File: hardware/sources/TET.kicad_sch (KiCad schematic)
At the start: 68 parts, among them J1 SWT, M1 MountingHole, M2 MountingHole, M3 MountingHole, M4 MountingHole, U1 E80-900M2213S_C42464134, U10 STM32L431RBT6TR, U12 TCAN330GDCNR, U13 SMA_1, U14 SMA_2, U15 8 MHz, U16 5015, U17 5015, U18 5015, U2 STM32L431CBT6, U3 W25Q128JVSIQTR, U4 W25Q128JVSIQTR, U5 W25Q128JVSIQTR, U6 TMP112AIDRLR, U7 TMP112AIDRLR, U8 TMP112AIDRLR, U9 TMP112AIDRLR

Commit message: hardware(schematics): upload pre-review schematic
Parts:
- removed C1, C14, C15, C16, C17, C18, C19: 100nF, Capacitor_SMD:C_0603_1608Metric, symbol Device:C_Small
- removed C20: 10uF, Capacitor_SMD:C_0603_1608Metric, symbol Device:C_Small
- removed C21: 10nF, Capacitor_SMD:C_0603_1608Metric, symbol Device:C_Small
- removed C22, C23: 1uF, Capacitor_SMD:C_0603_1608Metric, symbol Device:C_Small
- removed C8: 0.1uF, Capacitor_SMD:C_0603_1608Metric, symbol Device:C_Small
- removed D4: ON_LED, LED_SMD:LED_0805_2012Metric, symbol Device:LED
- removed D5: TX_LED, LED_SMD:LED_0805_2012Metric, symbol Device:LED
- removed D6: RX_LED, LED_SMD:LED_0805_2012Metric, symbol Device:LED
- removed J1: SWT, Connector_PinHeader_2.54mm:PinHeader_1x04_P2.54mm_Vertical, symbol Connector_Generic:Conn_01x04
- removed R3, R4: 10k, symbol Device:R_Small
- removed R6: 5k, Resistor_SMD:R_0603_1608Metric, symbol Device:R_Small
- removed U1: E80-900M2213S_C42464134, TET-Footprints:WIFIM-SMD_22P-L26.0-W16.0-P1.27-TL, symbol TET-Symbols:E80-900M2213S_C42464134
- removed U13: SMA_1, TET-Footprints:SMA-TH_SMA-KWE_C7498154, symbol TET-Symbols:SMA-KWE_C7498154
- removed U14: SMA_2, TET-Footprints:SMA-TH_SMA-KWE_C7498154, symbol TET-Symbols:SMA-KWE_C7498154
- removed U15: 8 MHz, TET-Footprints:CRYSTAL-SMD_L5.0-W3.2, symbol TET-Symbols:X50328MSB2GI
- removed U16, U17, U18: 5015, TET-Footprints:TEST-SMD_L2.7-W1.0, symbol TET-Symbols:5015
- removed U2: STM32L431CBT6, TET-Footprints:LQFP-48_L7.0-W7.0-P0.50-LS9.0-BL, symbol TET-Symbols:STM32L431CBT6
- removed U3, U4, U5: W25Q128JVSIQTR, TET-Footprints:SOIC-8_L5.3-W5.3-P1.27-LS8.0-BL, symbol TET-Symbols:W25Q128JVSIQTR
- removed U6, U8, U9: TMP112AIDRLR, TET-Footprints:SOT-563_L1.6-W1.2-P0.50-LS1.6-BR, symbol TET-Symbols:TMP112AIDRLR
- added C11: 10nF, Capacitor_SMD:C_0603_1608Metric, symbol Device:C_Small
- added C12: 1uF, Capacitor_SMD:C_0603_1608Metric, symbol Device:C_Small
- added C5: 100nF, Capacitor_SMD:C_0603_1608Metric, symbol Device:C_Small
- added J1: SWD, Connector_PinHeader_2.54mm:PinHeader_1x06_P2.54mm_Vertical, symbol Connector_Generic:Conn_01x06
- added R16: 10k, Resistor_SMD:R_0603_1608Metric, symbol Device:R_Small
- added R17, R7: 4.7k, Resistor_SMD:R_0603_1608Metric, symbol Device:R_Small
- added U2: 8 MHz, TET-Footprints:CRYSTAL-SMD_L5.0-W3.2, symbol TET-Symbols:X50328MSB2GI
- C10, C6, C7, C9: value 0.1uF -> 100nF
- C13: value 22uF -> 1uF
- C3: value 20pF -> 100nF
- C4: value 0.1uF -> 20pF
- FB1: LCSC C14709 -> (none)
- R1, R2, R5: footprint (none) -> Resistor_SMD:R_0603_1608Metric
- R10: value 200 -> 33
- R11: value 82 -> 33
- R12, R13: value 10k -> 33
- R14: value 10k -> 4.7k
- R15: value 5k -> 10k
- R3: renamed from R16; footprint Resistor_SMD:R_0805_2012Metric_Pad1.20x1.40mm_HandSolder -> Resistor_SMD:R_0603_1608Metric
- R4: renamed from R17; footprint Resistor_SMD:R_0805_2012Metric_Pad1.20x1.40mm_HandSolder -> Resistor_SMD:R_0603_1608Metric
- R6: renamed from R7; value 5k -> 4.7k
- R8: value 5k -> 4.7k
- R9: value 270 -> 33
- renumbered C11 to C1, C5 to C14, C12 to C8, U12 to U1, U10 to U3, U7 to U4
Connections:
- net BOOT0 is gone; now on net LR_NSS: R1.2
- net OSC_IN is gone; now on an unnamed net: C2.1
- net OSC_OUT is gone; now on net +3.3V: C3.1
- net TMP112_A_ALERT is gone; now on net I2C2_SCL: R8.2
- net +3.3V: now also R1.1, U3.1 (VBAT), U3.19 (VDD), U3.32 (VDD), U3.48 (VDD), U3.64 (VDD), C5.1, J1.1 (Pin_1), R16.1, R17.1, R7.1; no longer C4.1, C6.1, R12.1, R13.1, R5.1
- net +3.3VA: now also U3.13 (VDDA/VREF+), C11.1, C12.1
- net CAN1_RX: now also U3.44 (PA11)
- net CAN1_STB: now also U3.28 (PB2)
- net CAN1_TX: now also U3.45 (PA12)
- net FLASH1_CS: now also R15.2, U3.33 (PB12); no longer R12.2
- net FLASH2_CS: now also U3.34 (PB13), R16.2; no longer R13.2
- net FLASH3_CS: now also R18.2, U3.36 (PB15); no longer R14.2
- net GND: now also R5.1, U3.12 (VSSA/VREF-), U3.18 (VSS), U3.31 (VSS), U3.47 (VSS), U3.63 (VSS), C11.2, C12.2, C5.2, J1.6 (Pin_6); no longer R1.1, R10.1, R11.1, R9.1
- net I2C1_SCL: now also U3.58 (PB6), R7.2
- net I2C1_SDA: now also R14.2, U3.59 (PB7)
- net LR_BUSY: now also U3.40 (PC9)
- net LR_IO7: now also U3.52 (PC11)
- net LR_IO8: now also U3.53 (PC12)
- net LR_IO9: now also U3.2 (PC13)
- net LR_NSS: now also U3.51 (PC10)
- net LR_RST: now also R2.2, U3.39 (PC8); no longer R18.2
- net NRST: now also C6.1, U3.7 (NRST), J1.4 (Pin_4)
- net QSPI_CLK: now also R9.2
- net QSPI_IO0: now also R13.2
- net QSPI_IO1: now also R12.2
- net QSPI_IO2: now also R11.2
- net QSPI_IO3: now also R10.2
- net RX_LED: now also U3.9 (PC1)
- net SPI1_MISO: now also U3.56 (PB4)
- net SPI1_MOSI: now also U3.57 (PB5)
- net SPI1_SCK: now also U3.15 (PA1)
- net SWCLK: now also U3.49 (PA14), J1.3 (Pin_3)
- net SWDIO: now also U3.46 (PA13), J1.2 (Pin_2)
- net TX_LED: now also U3.8 (PC0)
- net RF_INA_ALERT: now reaches U3.14 (PA0)
- net TMP_B_ALERT: now reaches U3.16 (PA2)
- net TMP_B_ALERT: now also R6.2, U4.3 (ALERT)
- net at U3.17 (PA3): now also R9.1
- net TMP_C_ALERT: now reaches U3.20 (PA4)
- net TMP_D_ALERT: now reaches U3.21 (PA5)
- net at U3.22 (PA6): now also R10.1
- net at U3.23 (PA7): now also R11.1
- net UART_B_TX: now reaches U3.24 (PC4)
- net UART_B_RX: now reaches U3.25 (PC5)
- net at U3.26 (PB0): now also R12.1
- net at U3.27 (PB1): now also R13.1
- net I2C2_SCL: now reaches U3.29 (PB10)
- net I2C2_SDA: now reaches U3.35 (PB14)
- net I2C2_SDA: now also R17.2
- net PWR_INA_ALERT: now reaches U3.37 (PC6)
- net TMP_A_ALERT: now reaches U3.38 (PC7)
- net UART_A_TX: now reaches U3.42 (PA9)
- net UART_A_RX: now reaches U3.43 (PA10)
- net at U3.5 (PH0/OSCIN): now also U2.2 (OSC2)
- net SWO: now reaches U3.55 (PB3)
- net SWO: now also J1.5 (Pin_5)
- net at U3.6 (PH1/OSCOUT): now also C4.1, U2.1 (OSC1)
- net at U3.60 (PH3/BOOT0): now also R5.2
- removed net TMP112_B_ALERT: R5.2, R6.2, U4.3 (ALERT)
- removed net TMP112_D_ALERT: R15.2, R2.2
- no-connect marks 6 -> 10
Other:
- added sheet RF_Transceiver (TET-RF-Transceiver.kicad_sch)
- sheet Power_Supply ports: added CAN_A_H, CAN_A_L, I2C1_SCL, I2C1_SDA, PWR_INA_ALERT, RX_LED, TMP_A_ALERT, TX_LED, UART_A_RX, UART_A_TX, UART_B_RX, UART_B_TX; removed none
- note added: "MCU"
- note added: "MECHANICAL HOLES"
- note added: "OPEN HARDWARE"
- note removed: "1x CAN BUS 1x UART 1x SPI 1x QUADSPI 1x I2C"
- note removed: "Adicionar resistores de terminação + pull up nas linhas QSPI"
- note removed: "CL = 2*(CL0-Cs) = 2*(20pF-10pF) = 20pF"
- note removed: "GREEN"
- note removed: "PULL UP 4.7K"
- note removed: "RED"
- note removed: "YELLOW"
- moved on the sheet: C1, C14, C8, M1, M2, M3, M4, R3, R4, R6, U1, U3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

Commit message: hardware(schematic): link datasheet to all main components #1
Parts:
- FB1: LCSC (none) -> C14709
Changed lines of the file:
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@@
 			)
 		)
-		(property "Datasheet" "https://atta.szlcsc.com/upload/public/pdf/source/20201224/C1509088_801C146548210414D75CA4C6AF5FD003.pdf"
+		(property "Datasheet" "https://www.ti.com/lit/gpn/TCAN330G"
 			(at 53.594 182.753 0)
 			(effects
@@
 			)
 		)
-		(property "Datasheet" "https://item.szlcsc.com/188416.html"
+		(property "Datasheet" "https://www.ti.com/lit/gpn/TMP112"
 			(at 185.674 143.383 0)
 			(effects
@@
 			)
 		)
-		(property "Datasheet" "~"
+		(property "Datasheet" "https://www.lcsc.com/datasheet/C14709.pdf"
 			(at 166.37 27.94 0)
 			(effects
@@
 			)
 		)
+		(property "LCSC" "C14709"
+			(at 166.37 27.94 90)
+			(effects
+				(font
+					(size 1.27 1.27)
+				)
+				(hide yes)
+			)
+		)
 		(pin "2"
 		)
@@
 			)
 		)
-		(property "Datasheet" "https://item.szlcsc.com/92458.html"
+		(property "Datasheet" "https://www.lcsc.com/datasheet/C2053549.pdf"
 			(at 122.174 84.836 0)
 			(effects

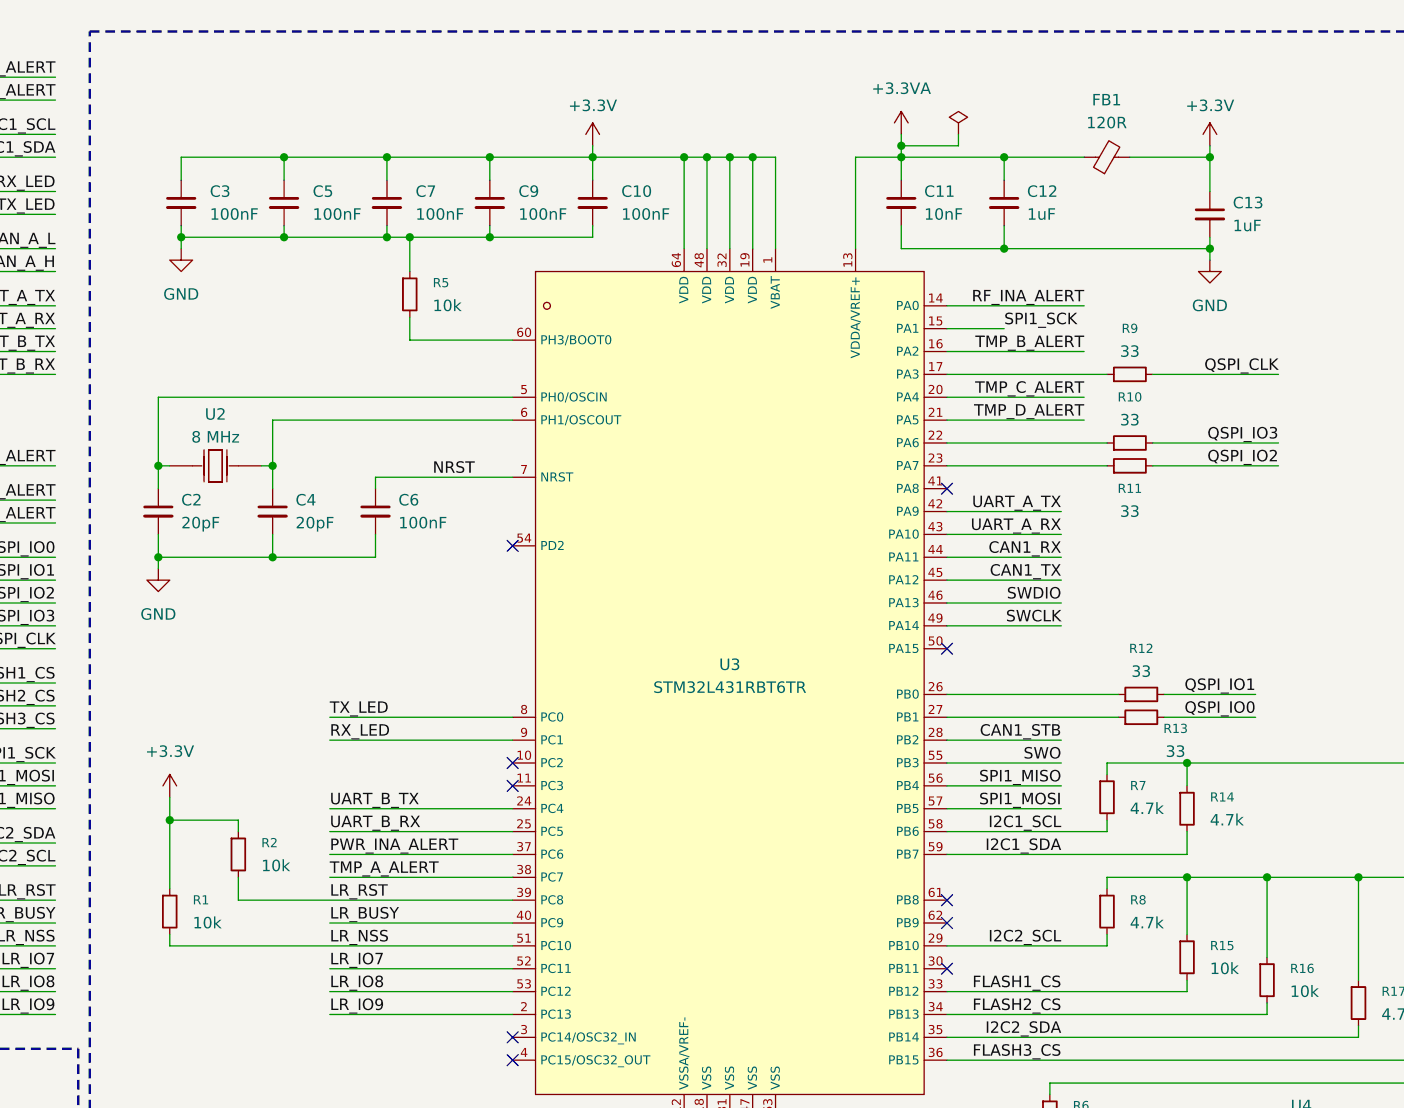
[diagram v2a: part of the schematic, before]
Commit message: hardware(schematic): fix Electrical Rules Check (ERC)
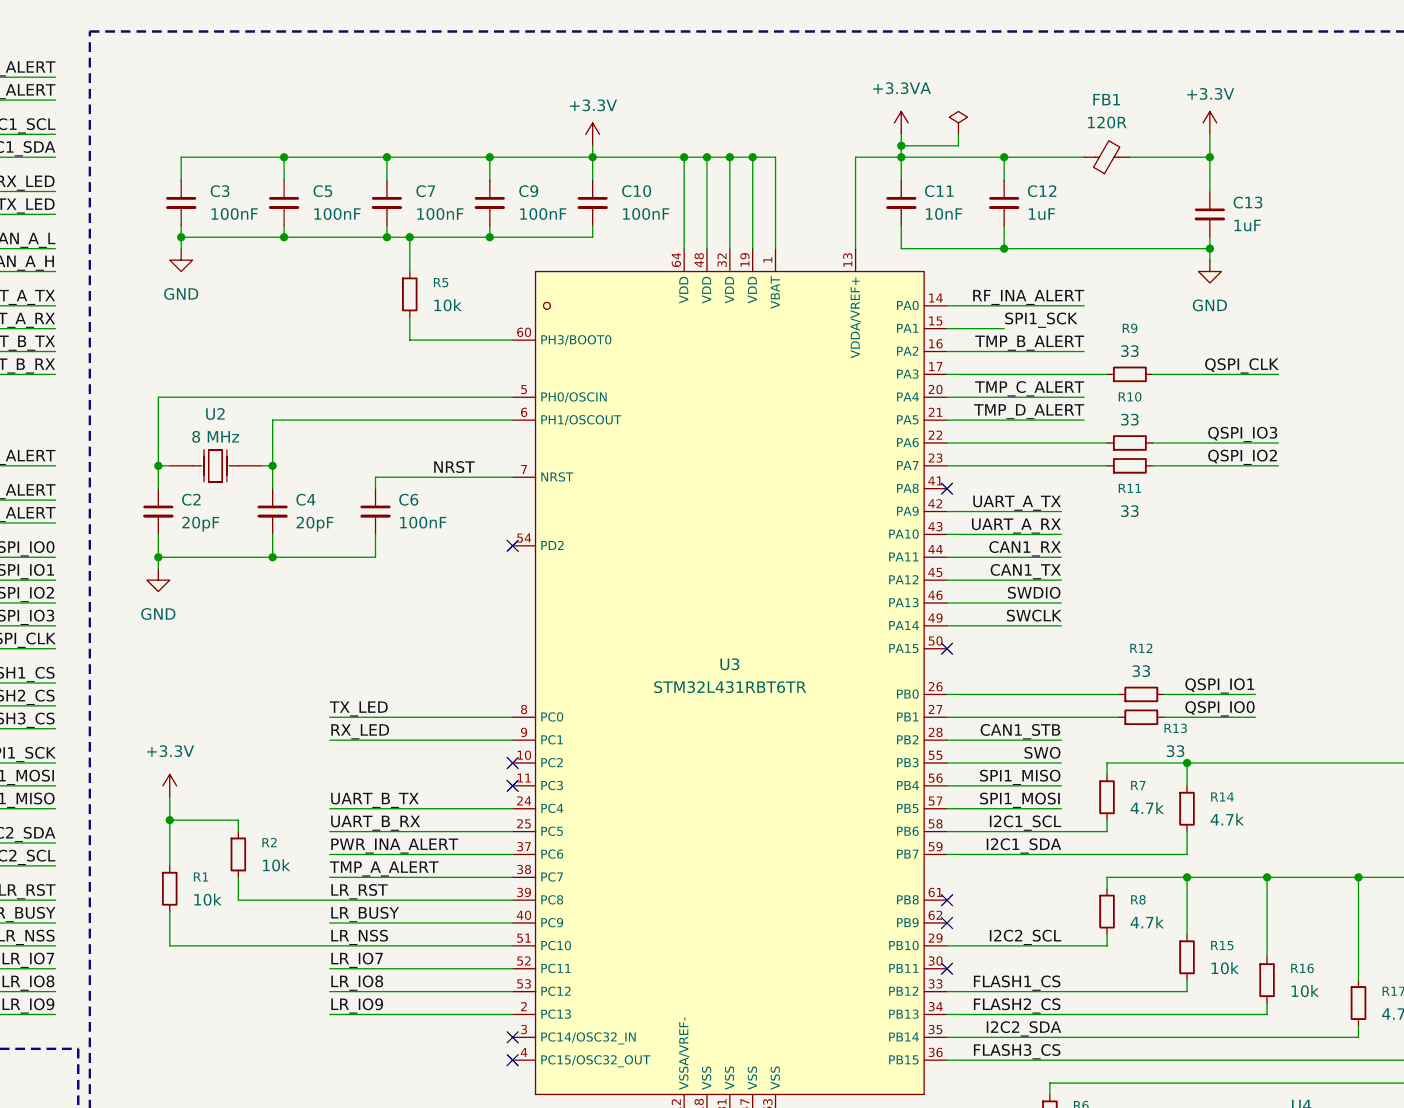
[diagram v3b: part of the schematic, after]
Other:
- moved on the sheet: R1
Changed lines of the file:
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@@
 	(wire
 		(pts
-			(xy 177.8 26.67) (xy 177.8 27.94)
+			(xy 177.8 25.4) (xy 177.8 27.94)
 		)
 		(stroke
@@
 	(wire
 		(pts
-			(xy 62.23 115.57) (xy 62.23 114.3)
+			(xy 62.23 115.57) (xy 62.23 111.76)
 		)
 		(stroke
@@
 	(wire
 		(pts
-			(xy 62.23 109.22) (xy 62.23 101.6)
+			(xy 62.23 106.68) (xy 62.23 101.6)
 		)
 		(stroke
@@
 	(symbol
 		(lib_id "power:+3.3V")
-		(at 177.8 26.67 0)
+		(at 177.8 25.4 0)
 		(unit 1)
 		(exclude_from_sim no)
@@
 		(fields_autoplaced yes)
 		(property "Reference" "#PWR09"
-			(at 177.8 30.48 0)
+			(at 177.8 29.21 0)
 			(effects
 				(font
@@
 		)
 		(property "Value" "+3.3V"
-			(at 177.8 22.225 0)
+			(at 177.8 20.955 0)
 			(effects
 				(font
@@
 		)
 		(property "Footprint" ""
-			(at 177.8 26.67 0)
+			(at 177.8 25.4 0)
 			(effects
 				(font
@@
 		)
 		(property "Datasheet" ""
-			(at 177.8 26.67 0)
+			(at 177.8 25.4 0)
 			(effects
 				(font
@@
 		)
 		(property "Description" "Power symbol creates a global label with name \"+3.3V\""
-			(at 177.8 26.67 0)
+			(at 177.8 25.4 0)
 			(effects
 				(font
@@
 	(symbol
 		(lib_id "Device:R_Small")
-		(at 62.23 111.76 0)
+		(at 62.23 109.22 0)
 		(unit 1)
 		(exclude_from_sim no)
@@
 		(fields_autoplaced yes)
 		(property "Reference" "R1"
-			(at 64.77 110.4899 0)
+			(at 64.77 107.9499 0)
 			(effects
 				(font
@@
 		)
 		(property "Value" "10k"
-			(at 64.77 113.0299 0)
+			(at 64.77 110.4899 0)
 			(effects
 				(font
@@
 		)
 		(property "Footprint" "Resistor_SMD:R_0603_1608Metric"
-			(at 62.23 111.76 0)
+			(at 62.23 109.22 0)
 			(effects
 				(font
@@
 		)
 		(property "Datasheet" "~"
-			(at 62.23 111.76 0)
+			(at 62.23 109.22 0)
 			(effects
 				(font
@@
 		)
 		(property "Description" "Resistor, small symbol"
-			(at 62.23 111.76 0)
+			(at 62.23 109.22 0)
 			(effects
 				(font

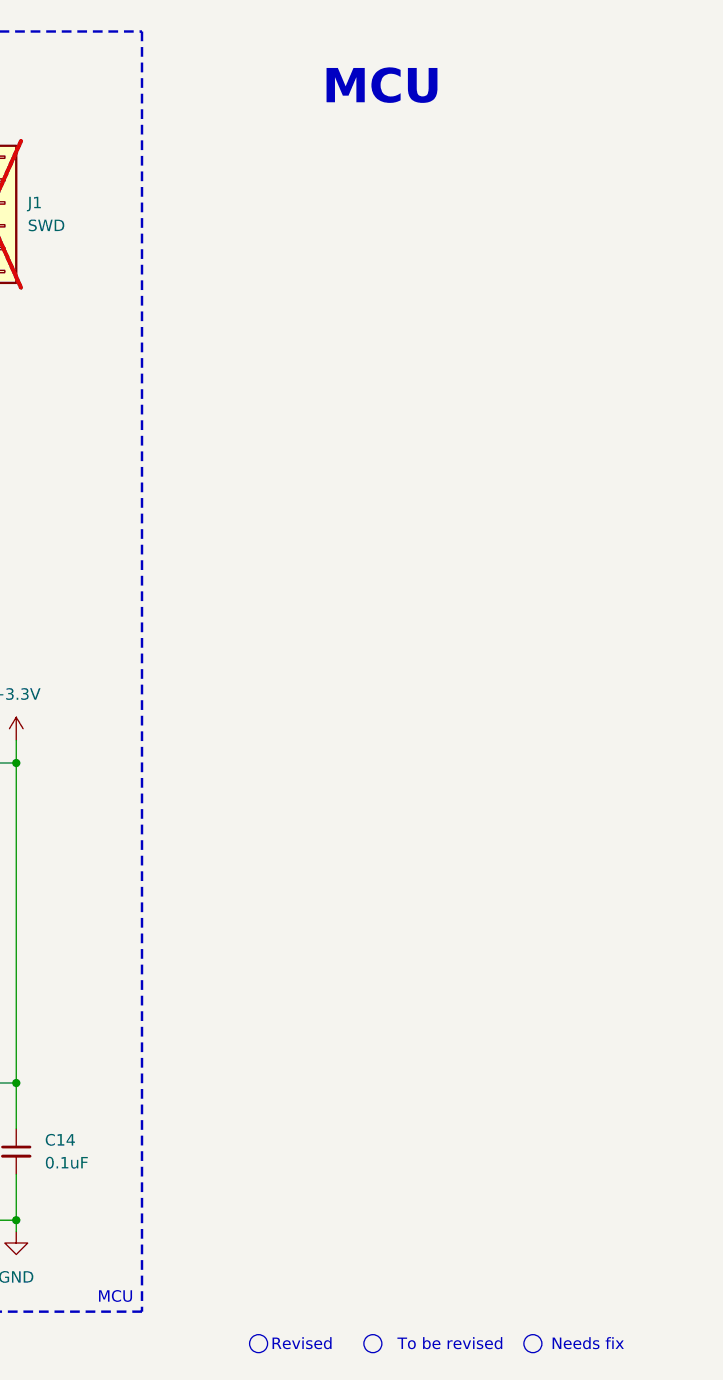
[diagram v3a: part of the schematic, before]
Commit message: hardware(schematic): update documentation for all sheets
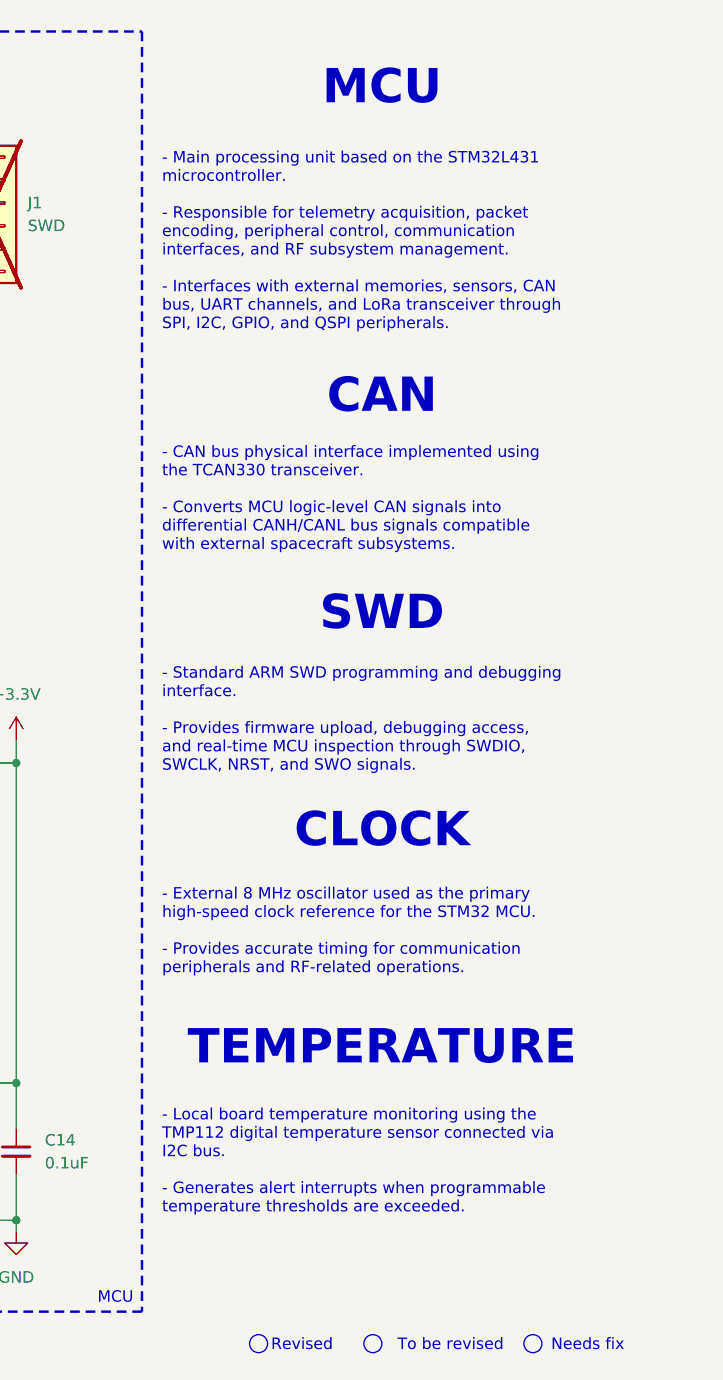
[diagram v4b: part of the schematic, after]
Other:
- note added: "CAN"
- note added: "CLOCK"
- note added: "SWD"
- note added: "TEMPERATURE"
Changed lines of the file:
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@@
+		)
+	)
+	(text "SWD"
+		(exclude_from_sim no)
+		(at 256.54 78.74 0)
+		(effects
+			(font
+				(size 3.81 3.81)
+				(thickness 0.762)
+				(bold yes)
+			)
 		)
 	)
@@
 				(size 1.27 1.27)
 				(color 0 194 0 1)
+			)
+		)
+	)
+	(text "TEMPERATURE"
+		(exclude_from_sim no)
+		(at 256.54 127 0)
+		(effects
+			(font
+				(size 3.81 3.81)
+				(thickness 0.762)
+				(bold yes)
 			)
 		)
@@
 		)
 	)
+	(text "CLOCK"
+		(exclude_from_sim no)
+		(at 256.54 102.87 0)
+		(effects
+			(font
+				(size 3.81 3.81)
+				(thickness 0.762)
+				(bold yes)
+			)
+		)
+	)
 	(text "MECHANICAL HOLES"
 		(exclude_from_sim no)
@@
 				(size 1.27 1.27)
 				(color 255 153 0 1)
+			)
+		)
+	)
+	(text "CAN"
+		(exclude_from_sim no)
+		(at 256.54 54.61 0)
+		(effects
+			(font
+				(size 3.81 3.81)
+				(thickness 0.762)
+				(bold yes)
 			)
 		)
@@
 		)
 	)
-	(text_box ""
+	(text_box "\n\n\n\n\n\n- Main processing unit based on the STM32L431 microcontroller.\n\n- Responsible for telemetry acquisition, packet encoding, peripheral control, communication interfaces, and RF subsystem management.\n\n- Interfaces with external memories, sensors, CAN bus, UART channels, and LoRa transceiver through SPI, I2C, GPIO, and QSPI peripherals.\n\n\n\n\n\n\n- CAN bus physical interface implemented using the TCAN330 transceiver.\n\n- Converts MCU logic-level CAN signals into differential CANH/CANL bus signals compatible with external spacecraft subsystems.\n\n\n\n\n\n\n- Standard ARM SWD programming and debugging interface.\n\n- Provides firmware upload, debugging access, and real-time MCU inspection through SWDIO, SWCLK, NRST, and SWO signals.\n\n\n\n\n\n\n- External 8 MHz oscillator used as the primary high-speed clock reference for the STM32 MCU.\n\n- Provides accurate timing for communication peripherals and RF-related operations.\n\n\n\n\n\n\n\n- Local board temperature monitoring using the TMP112 digital temperature sensor connected via I2C bus.\n\n- Generates alert interrupts when programmable temperature thresholds are exceeded.\n\n"
 		(exclude_from_sim no)
 		(at 231.14 13.97 0)
